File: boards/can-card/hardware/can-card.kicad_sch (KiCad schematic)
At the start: 77 parts, among them J10 STACK BUS, J11 RACK 12V, J21 CAN1, J22 CAN2, J23 CAN3, J24 CAN4, U10 ISOW1044, U11 ISOW1044, U12 ISOW1044, U13 ISOW1044

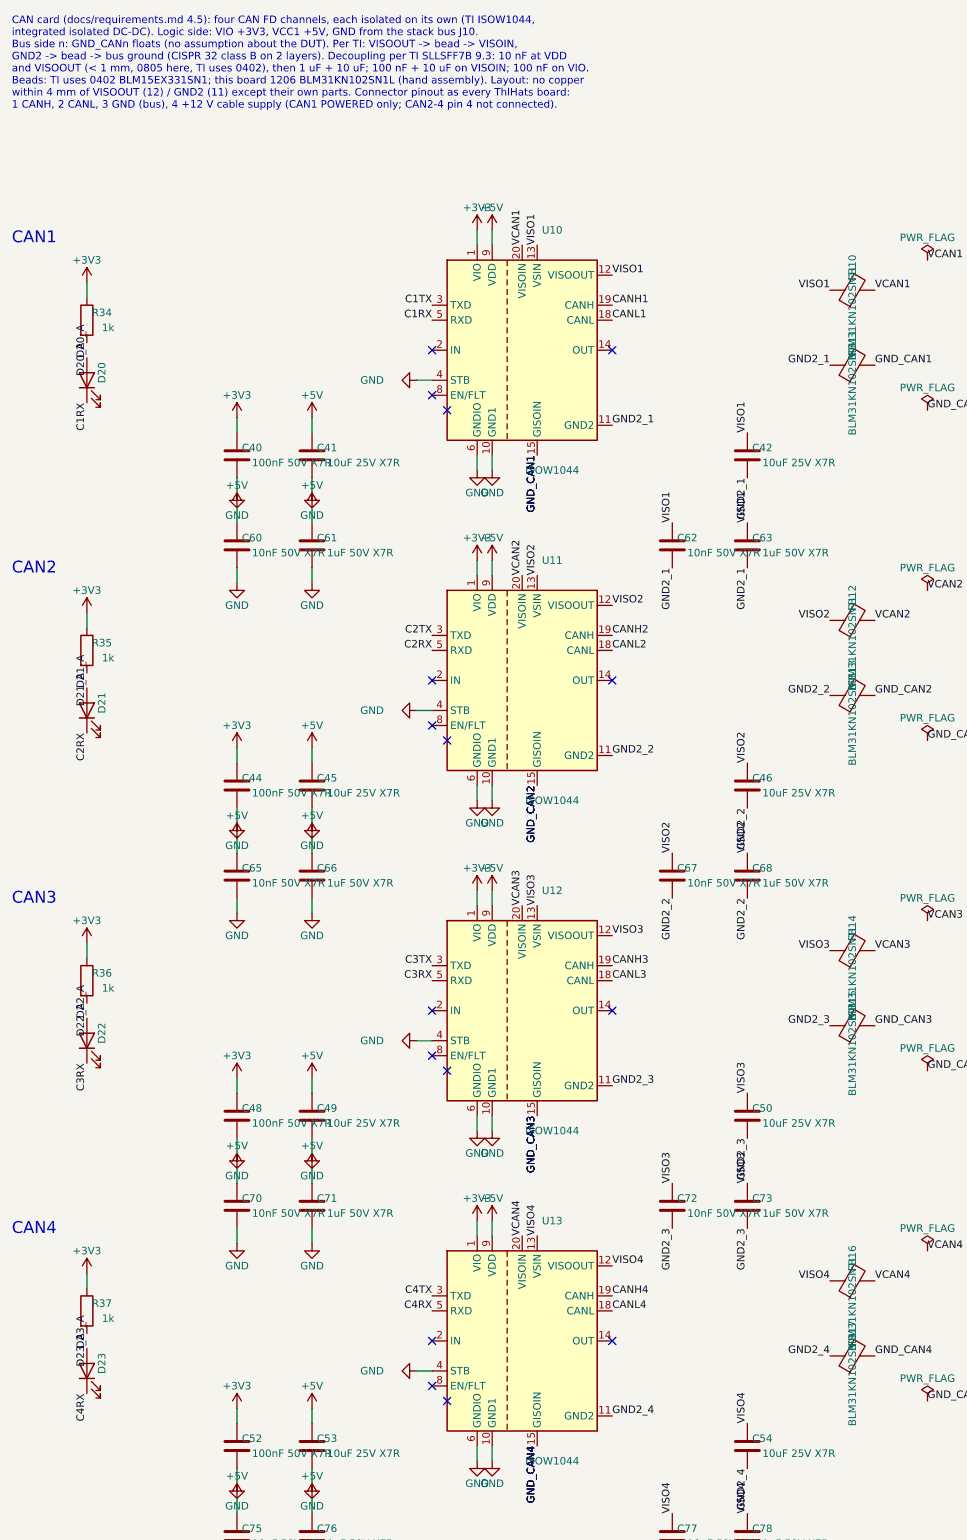
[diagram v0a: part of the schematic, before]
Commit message: Move core, can-card, io-card, serial-card, can-ssr, probe-helper to rev B
Rev A went to PCBWay and is tagged revA. Rev B replaces parts the Mouser
BOM check flagged (obsolete, end of life, not recommended for new designs,
or not orderable) and swaps out-of-stock passives and diodes for in-stock
equivalents. Field-only changes, same footprints, no layout change; the
reference boards (can-controller, pic-module) get the same part numbers.
The rev A order lists (DigiKey, Mouser) carry the same substitutions; the
Mouser list leaves out the T821 box headers (bought from DigiKey).

docs/rev-b-changes.md lists every change and the rev B to-dos (MAX7219 is
obsolete and must be replaced). transfer/mouser-revA.xlsx (Mouser BOM
check) consumed.

Co-Authored-By: Claude Opus 5.5 <noreply@anthropic.com>
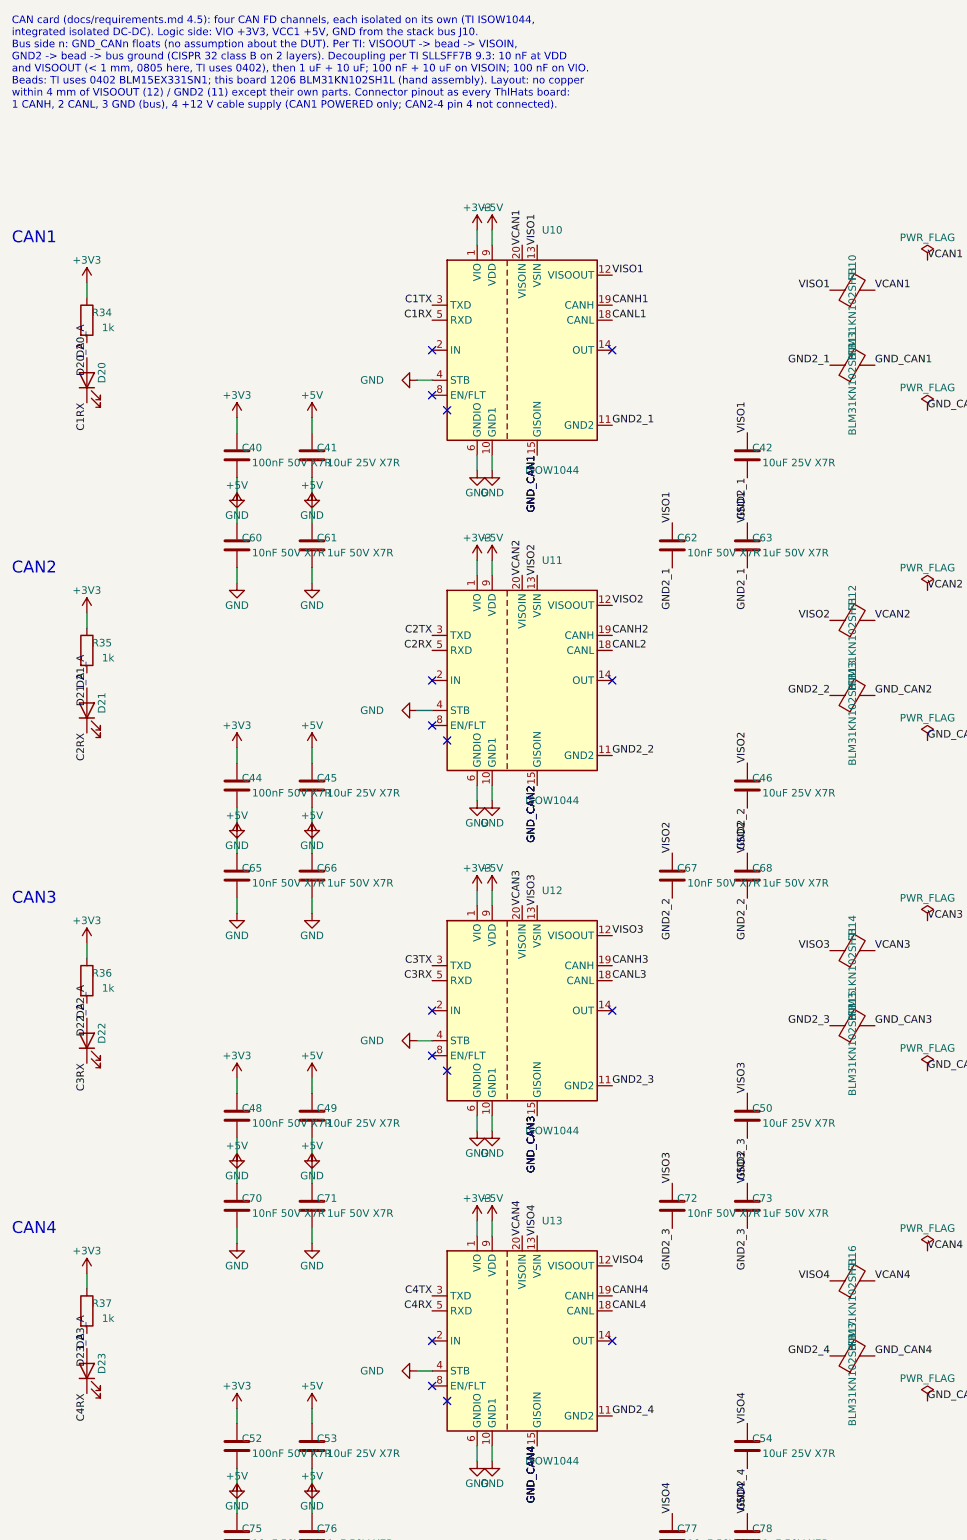
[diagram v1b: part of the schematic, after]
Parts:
- C40, C43, C44, C47, C48, C51, C52, C55: MPN GRM21BR71H104KA01L -> C0805C104K5RACTU; Manufacturer Murata -> KEMET
- C41, C42, C45, C46, C49, C50, C53, C54, C64, C69, C74, C79: MPN GRM31CR71E106KA12L -> CL31B106KAHNNNE; Manufacturer Murata -> Samsung Electro-Mechanics
- C60, C62, C65, C67, C70, C72, C75, C77: MPN GRM21BR71H103KA01L -> C0805C103K5RACTU; Manufacturer Murata -> KEMET
- C61, C63, C66, C68, C71, C73, C76, C78: MPN GRM31MR71H105KA88L -> C1206C105K5RACTU; Manufacturer Murata -> KEMET
- FB10, FB11, FB12, FB13, FB14, FB15, FB16, FB17: value BLM31KN102SN1L -> BLM31KN102SH1L; MPN BLM31KN102SN1L -> BLM31KN102SH1L

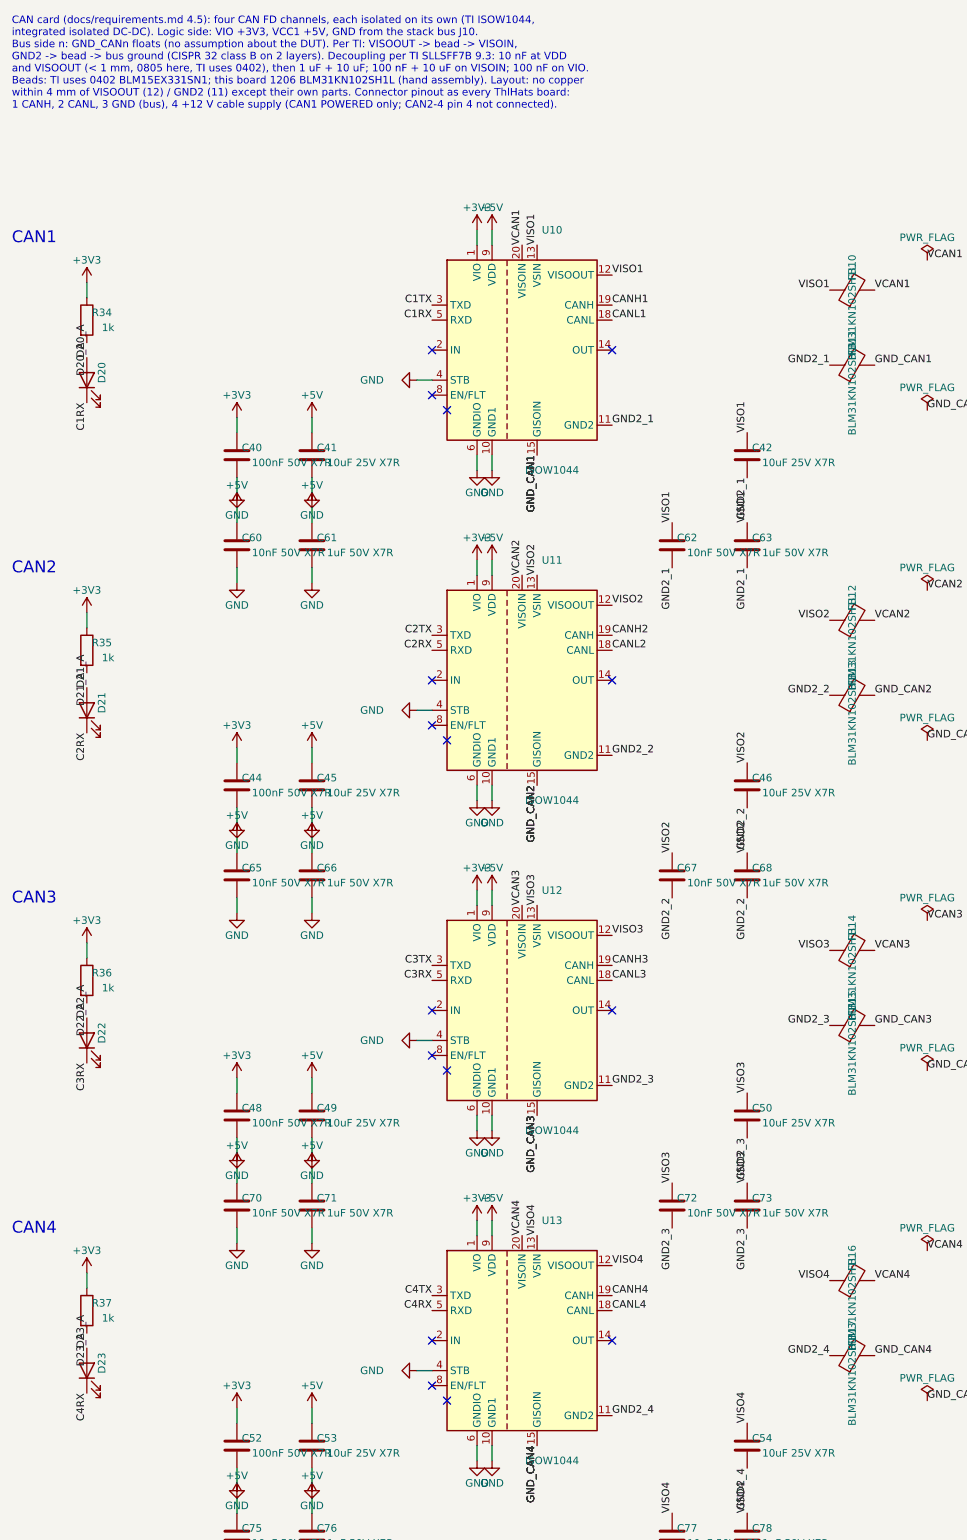
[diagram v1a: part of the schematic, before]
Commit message: Rev B / rev A order: 10 uF CL31B106KAHZW6E, beads BLM31PG391SN1L
Both earlier substitutes (CL31B106KAHNNNE, BLM31KN102SH1L) are on
backorder at Mouser. CL31B106KAHZW6E has the same rating (1.4 mm tall).
The isolated-supply beads need no 1 kOhm: TI's reference uses 330 Ohm;
BLM31PG391SN1L is 390 Ohm @ 100 MHz, 2 A, 50 mOhm. Field-only changes;
order lists regenerated.

Co-Authored-By: Claude Opus 5.5 <noreply@anthropic.com>
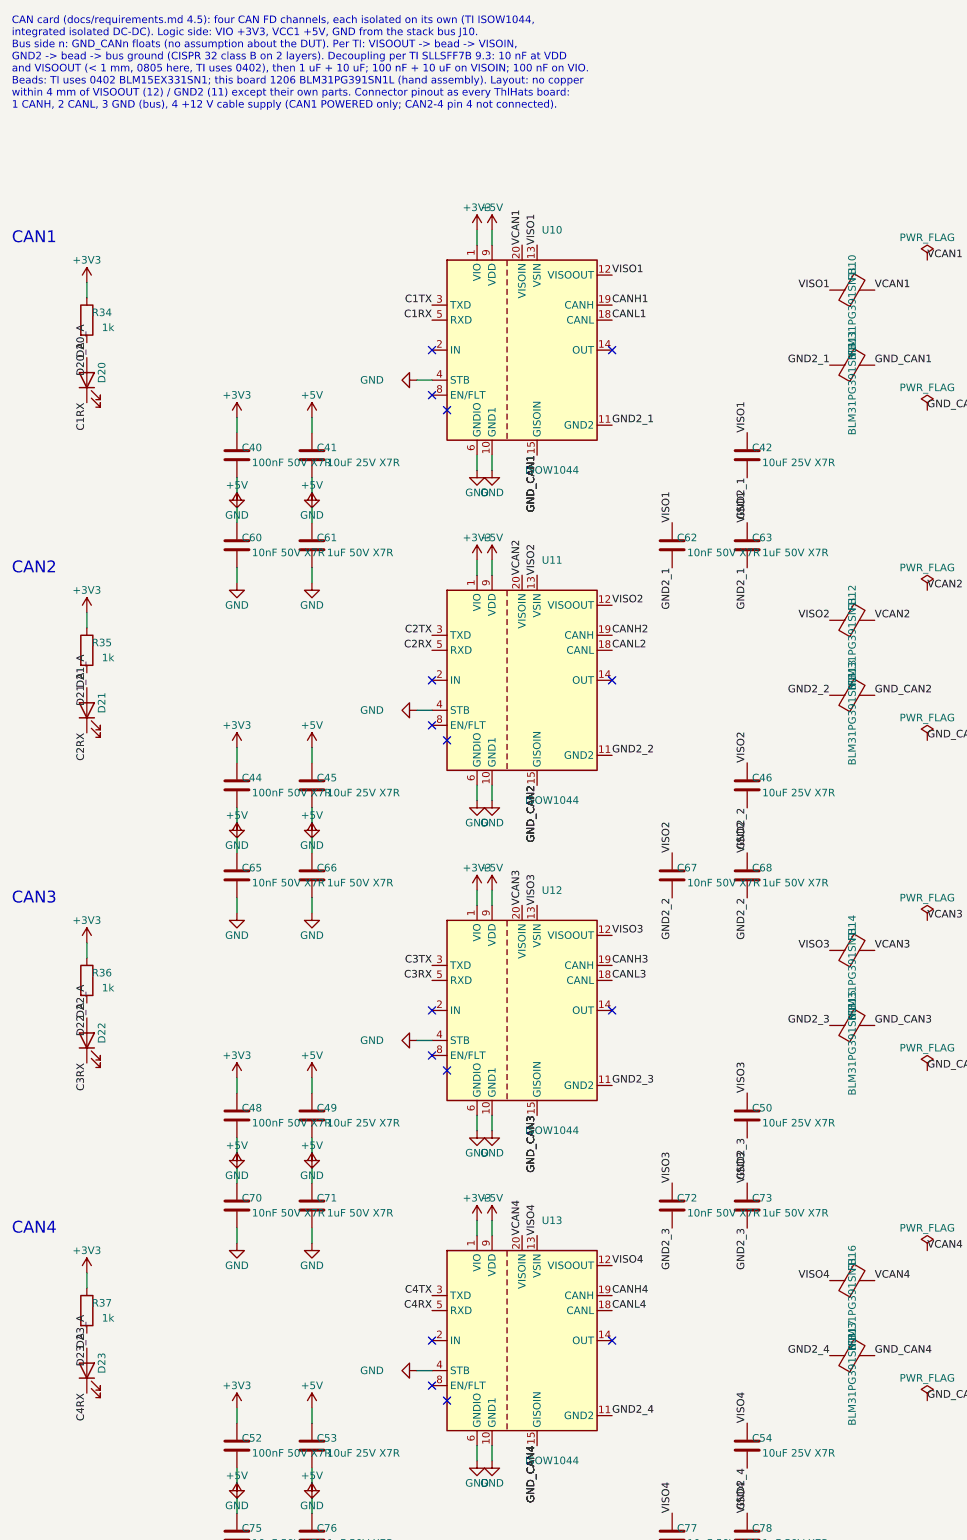
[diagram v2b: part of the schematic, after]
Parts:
- C41, C42, C45, C46, C49, C50, C53, C54, C64, C69, C74, C79: MPN CL31B106KAHNNNE -> CL31B106KAHZW6E
- FB10, FB11, FB12, FB13, FB14, FB15, FB16, FB17: value BLM31KN102SH1L -> BLM31PG391SN1L; MPN BLM31KN102SH1L -> BLM31PG391SN1L
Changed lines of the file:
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@@
 		(rev "B")
 	)
-	(text "CAN card (docs/requirements.md 4.5): four CAN FD channels, each isolated on its own (TI ISOW1044,\nintegrated isolated DC-DC). Logic side: VIO +3V3, VCC1 +5V, GND from the stack bus J10.\nBus side n: GND_CANn floats (no assumption about the DUT). Per TI: VISOOUT -> bead -> VISOIN,\nGND2 -> bead -> bus ground (CISPR 32 class B on 2 layers). Decoupling per TI SLLSFF7B 9.3: 10 nF at VDD\nand VISOOUT (< 1 mm, 0805 here, TI uses 0402), then 1 uF + 10 uF; 100 nF + 10 uF on VISOIN; 100 nF on VIO.\nBeads: TI uses 0402 BLM15EX331SN1; this board 1206 BLM31KN102SH1L (hand assembly). Layout: no copper\nwithin 4 mm of VISOOUT (12) / GND2 (11) except their own parts. Connector pinout as every ThlHats board:\n1 CANH, 2 CANL, 3 GND (bus), 4 +12 V cable supply (CAN1 POWERED only; CAN2-4 pin 4 not connected)."
+	(text "CAN card (docs/requirements.md 4.5): four CAN FD channels, each isolated on its own (TI ISOW1044,\nintegrated isolated DC-DC). Logic side: VIO +3V3, VCC1 +5V, GND from the stack bus J10.\nBus side n: GND_CANn floats (no assumption about the DUT). Per TI: VISOOUT -> bead -> VISOIN,\nGND2 -> bead -> bus ground (CISPR 32 class B on 2 layers). Decoupling per TI SLLSFF7B 9.3: 10 nF at VDD\nand VISOOUT (< 1 mm, 0805 here, TI uses 0402), then 1 uF + 10 uF; 100 nF + 10 uF on VISOIN; 100 nF on VIO.\nBeads: TI uses 0402 BLM15EX331SN1; this board 1206 BLM31PG391SN1L (hand assembly). Layout: no copper\nwithin 4 mm of VISOOUT (12) / GND2 (11) except their own parts. Connector pinout as every ThlHats board:\n1 CANH, 2 CANL, 3 GND (bus), 4 +12 V cable supply (CAN1 POWERED only; CAN2-4 pin 4 not connected)."
 		(exclude_from_sim no)
 		(at 25.4 22.86 0)
@@
 			)
 		)
-		(property "MPN" "CL31B106KAHNNNE"
+		(property "MPN" "CL31B106KAHZW6E"
 			(at 76.2 81.28 0)
 			(hide yes)
@@
 			)
 		)
-		(property "MPN" "CL31B106KAHNNNE"
+		(property "MPN" "CL31B106KAHZW6E"
 			(at 149.86 81.28 0)
 			(hide yes)
@@
 			)
 		)
-		(property "MPN" "CL31B106KAHNNNE"
+		(property "MPN" "CL31B106KAHZW6E"
 			(at 193.04 96.52 0)
 			(hide yes)
@@
 			)
 		)
-		(property "Value" "BLM31KN102SH1L"
+		(property "Value" "BLM31PG391SN1L"
 			(at 167.64 57.15 0)
 			(effects
@@
 			)
 		)
-		(property "MPN" "BLM31KN102SH1L"
+		(property "MPN" "BLM31PG391SN1L"
 			(at 167.64 53.34 0)
 			(hide yes)
@@
 			)
 		)
-		(property "Value" "BLM31KN102SH1L"
+		(property "Value" "BLM31PG391SN1L"
 			(at 167.64 69.85 0)
 			(effects
@@
 			)
 		)
-		(property "MPN" "BLM31KN102SH1L"
+		(property "MPN" "BLM31PG391SN1L"
 			(at 167.64 66.04 0)
 			(hide yes)
@@
 			)
 		)
-		(property "MPN" "CL31B106KAHNNNE"
+		(property "MPN" "CL31B106KAHZW6E"
 			(at 76.2 137.16 0)
 			(hide yes)
@@
 			)
 		)
-		(property "MPN" "CL31B106KAHNNNE"
+		(property "MPN" "CL31B106KAHZW6E"
 			(at 149.86 137.16 0)
 			(hide yes)
@@
 			)
 		)
-		(property "MPN" "CL31B106KAHNNNE"
+		(property "MPN" "CL31B106KAHZW6E"
 			(at 193.04 152.4 0)
 			(hide yes)
@@
 			)
 		)
-		(property "Value" "BLM31KN102SH1L"
+		(property "Value" "BLM31PG391SN1L"
 			(at 167.64 113.03 0)
 			(effects
@@
 			)
 		)
-		(property "MPN" "BLM31KN102SH1L"
+		(property "MPN" "BLM31PG391SN1L"
 			(at 167.64 109.22 0)
 			(hide yes)
@@
 			)
 		)
-		(property "Value" "BLM31KN102SH1L"
+		(property "Value" "BLM31PG391SN1L"
 			(at 167.64 125.73 0)
 			(effects
@@
 			)
 		)
-		(property "MPN" "BLM31KN102SH1L"
+		(property "MPN" "BLM31PG391SN1L"
 			(at 167.64 121.92 0)
 			(hide yes)
@@
 			)
 		)
-		(property "MPN" "CL31B106KAHNNNE"
+		(property "MPN" "CL31B106KAHZW6E"
 			(at 76.2 193.04 0)
 			(hide yes)
@@
 			)
 		)
-		(property "MPN" "CL31B106KAHNNNE"
+		(property "MPN" "CL31B106KAHZW6E"
 			(at 149.86 193.04 0)
 			(hide yes)
@@
 			)
 		)
-		(property "MPN" "CL31B106KAHNNNE"
+		(property "MPN" "CL31B106KAHZW6E"
 			(at 193.04 208.28 0)
 			(hide yes)
@@
 			)
 		)
-		(property "Value" "BLM31KN102SH1L"
+		(property "Value" "BLM31PG391SN1L"
 			(at 167.64 168.91 0)
 			(effects
@@
 			)
 		)
-		(property "MPN" "BLM31KN102SH1L"
+		(property "MPN" "BLM31PG391SN1L"
 			(at 167.64 165.1 0)
 			(hide yes)
@@
 			)
 		)
-		(property "Value" "BLM31KN102SH1L"
+		(property "Value" "BLM31PG391SN1L"
 			(at 167.64 181.61 0)
 			(effects
@@
 			)
 		)
-		(property "MPN" "BLM31KN102SH1L"
+		(property "MPN" "BLM31PG391SN1L"
 			(at 167.64 177.8 0)
 			(hide yes)
@@
 			)
 		)
-		(property "MPN" "CL31B106KAHNNNE"
+		(property "MPN" "CL31B106KAHZW6E"
 			(at 76.2 248.92 0)
 			(hide yes)
@@
 			)
 		)
-		(property "MPN" "CL31B106KAHNNNE"
+		(property "MPN" "CL31B106KAHZW6E"
 			(at 149.86 248.92 0)
 			(hide yes)
@@
 			)
 		)
-		(property "MPN" "CL31B106KAHNNNE"
+		(property "MPN" "CL31B106KAHZW6E"
 			(at 193.04 264.16 0)
 			(hide yes)
@@
 			)
 		)
-		(property "Value" "BLM31KN102SH1L"
+		(property "Value" "BLM31PG391SN1L"
 			(at 167.64 224.79 0)
 			(effects
@@
 			)
 		)
-		(property "MPN" "BLM31KN102SH1L"
+		(property "MPN" "BLM31PG391SN1L"
 			(at 167.64 220.98 0)
 			(hide yes)
@@
 			)
 		)
-		(property "Value" "BLM31KN102SH1L"
+		(property "Value" "BLM31PG391SN1L"
 			(at 167.64 237.49 0)
 			(effects
@@
 			)
 		)
-		(property "MPN" "BLM31KN102SH1L"
+		(property "MPN" "BLM31PG391SN1L"
 			(at 167.64 233.68 0)
 			(hide yes)

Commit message: Rev B / rev A order: ISOW1044BDFMR (ISOW1044DFMR out of stock)
Same TI part, package and pinout with basic instead of reinforced
isolation; the CAN buses are low-voltage and isolated against ground
loops, not for safety. Field-only change on can-card (and the reference
can-controller); order lists regenerated.

Co-Authored-By: Claude Opus 5.5 <noreply@anthropic.com>
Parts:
- U10, U11, U12, U13: value ISOW1044 -> ISOW1044B; MPN ISOW1044DFMR -> ISOW1044BDFMR
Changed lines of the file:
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@@
 			)
 		)
-		(property "Value" "ISOW1044"
+		(property "Value" "ISOW1044B"
 			(at 116.84 83.82 0)
 			(effects
@@
 			)
 		)
-		(property "MPN" "ISOW1044DFMR"
+		(property "MPN" "ISOW1044BDFMR"
 			(at 111.76 63.5 0)
 			(hide yes)
@@
 			)
 		)
-		(property "Value" "ISOW1044"
+		(property "Value" "ISOW1044B"
 			(at 116.84 139.7 0)
 			(effects
@@
 			)
 		)
-		(property "MPN" "ISOW1044DFMR"
+		(property "MPN" "ISOW1044BDFMR"
 			(at 111.76 119.38 0)
 			(hide yes)
@@
 			)
 		)
-		(property "Value" "ISOW1044"
+		(property "Value" "ISOW1044B"
 			(at 116.84 195.58 0)
 			(effects
@@
 			)
 		)
-		(property "MPN" "ISOW1044DFMR"
+		(property "MPN" "ISOW1044BDFMR"
 			(at 111.76 175.26 0)
 			(hide yes)
@@
 			)
 		)
-		(property "Value" "ISOW1044"
+		(property "Value" "ISOW1044B"
 			(at 116.84 251.46 0)
 			(effects
@@
 			)
 		)
-		(property "MPN" "ISOW1044DFMR"
+		(property "MPN" "ISOW1044BDFMR"
 			(at 111.76 231.14 0)
 			(hide yes)
